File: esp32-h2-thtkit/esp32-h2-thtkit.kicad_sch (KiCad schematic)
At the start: 28 parts, among them J1 PIN_GROUP_1, J2 PIN_GROUP_3, J3 PIN_GROUP_2, J4 UART, U1 MIC5219-3.3YM5, U2 ESP32-H2, Y1 32.768kHz ±20ppm CL12.5pF, Y2 32MHz ±10ppm CL8pF

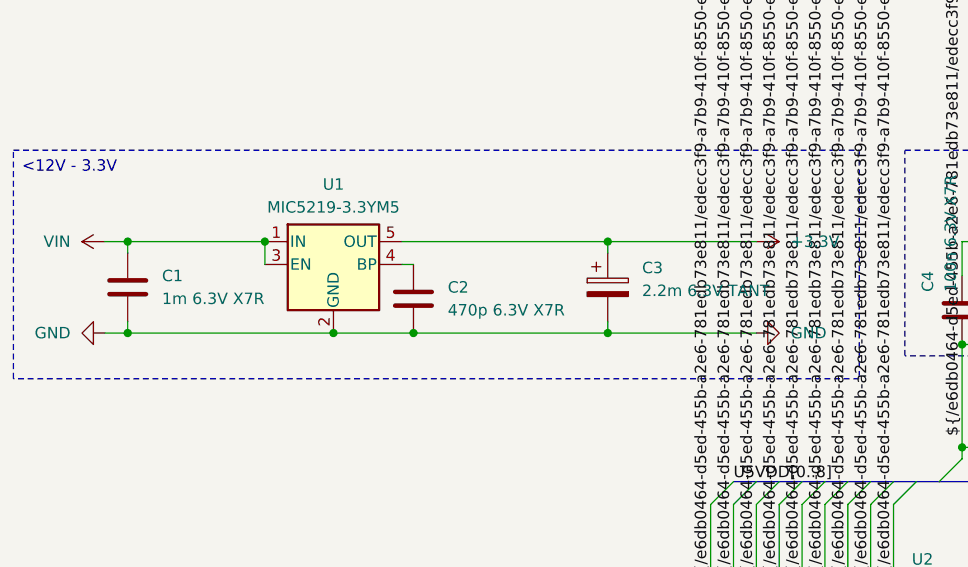
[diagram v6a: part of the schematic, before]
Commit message: Unify schemas and fix esp32-c3 footprint
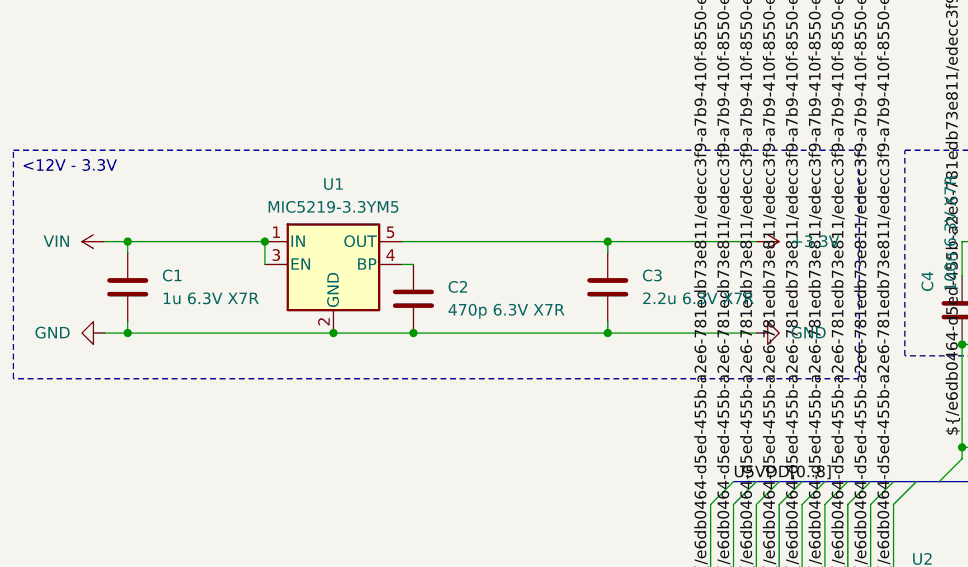
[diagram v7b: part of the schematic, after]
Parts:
- removed C3: 2.2m 6.3V TANT, Capacitor_Tantalum_SMD:CP_EIA-2012-12_Kemet-R, symbol Device:C_Polarized
- added C3: 2.2u 6.3V X7R, Capacitor_SMD:C_0402_1005Metric, symbol Device:C
- C1: value 1m 6.3V X7R -> 1u 6.3V X7R; Mouser PN DRAFT (none) -> 963-TMK105BJ105MV-F
- C10, C4, C5, C6, C9: Mouser PN DRAFT (none) -> 963-MLASU105SB7104KF
- C11, C14: Mouser PN DRAFT (none) -> 963-MCASU105SCG150JF
- C12, C13: Mouser PN DRAFT (none) -> 603-CC0402JRNPO9BN25
- C2: Mouser PN DRAFT (none) -> 963-MCASU105SB7471KF
- C7: Mouser PN DRAFT (none) -> 963-MCASU105SCG5R6CF
- C8: Mouser PN DRAFT (none) -> 963-MBASU105SCG2R2BF
- L1: Mouser PN DRAFT (none) -> 81-LQG15HS3N9B02D
- R1, R2: Mouser PN DRAFT (none) -> 667-ERJ-PA2D1002X
- U1: Mouser PN DRAFT (none) -> 998-MIC5219-3.3YM5TR
- U2: Mouser PN DRAFT (none) -> 356-ESP32-H2FH4
- Y1, Y2: Mouser PN DRAFT (none) -> 815-ABS05N32768KH9T5
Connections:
- net +3.3V: now also C3.2
- net GND: now also C3.1
